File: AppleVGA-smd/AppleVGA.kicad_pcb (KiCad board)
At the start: 2 copper layers, 112.4 x 66.7 mm, 35 parts, among them J1 AppleIIBus, J2 VGA, Q1 DMG2305UX-7, SW1 Reset, U1 74LVC245, U2 74LVC245, U3 74LVC245, U4 74LVC245, U6 Pico

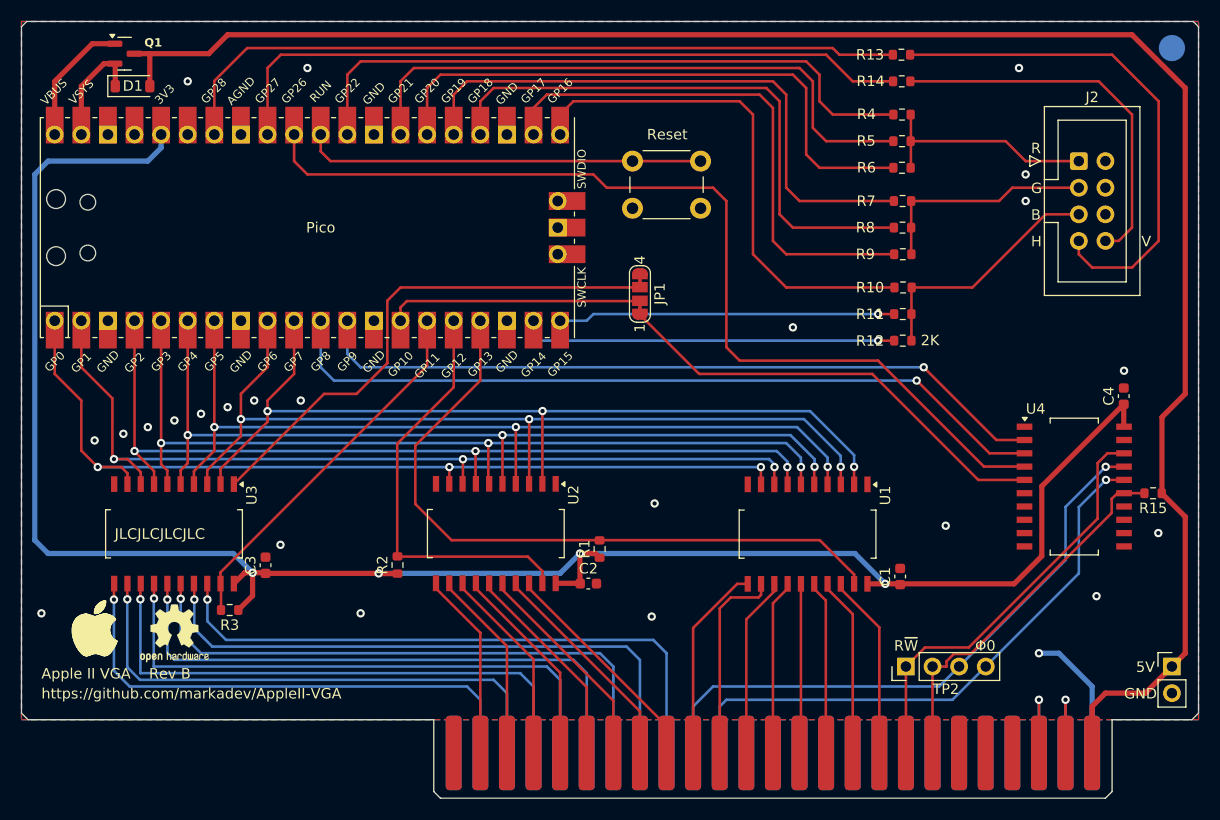
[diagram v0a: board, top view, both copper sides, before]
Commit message: Finalize SMD version
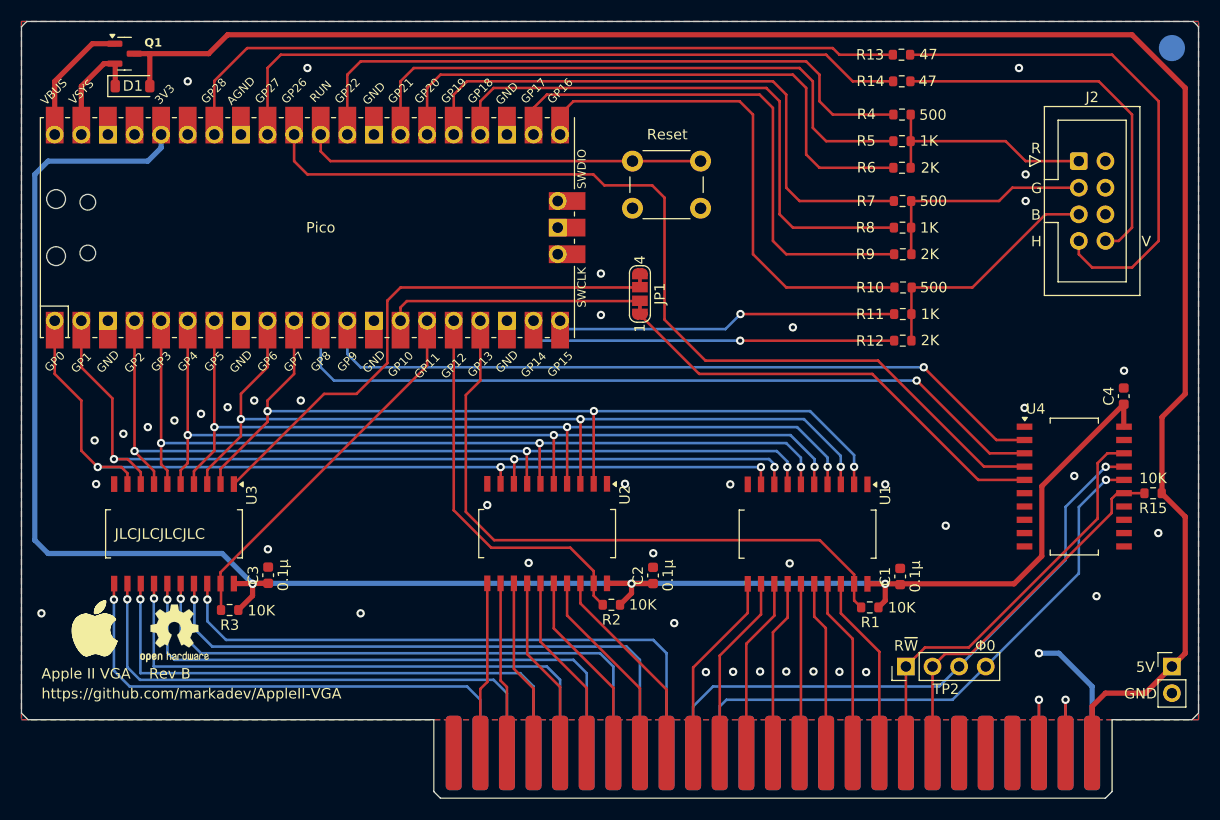
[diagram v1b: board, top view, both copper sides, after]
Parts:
- moved R1 26.4 mm to (161.7, 122.6), turned to 180 degrees
- moved R2 20.8 mm to (137.0, 122.4), turned to 180 degrees
- moved C2 6.22 mm to (140.9, 119.6), turned to 90 degrees
- moved U2 4.90 mm to (130.8, 115.6)
- moved C3 0.98 mm to (104.2, 119.5)
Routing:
- net Net-(U1-CE): track 65.7 -> 61.8 mm
- net Net-(U2-CE): track 40.4 -> 37.4 mm
- net /A2: track 19.6 -> 17.6 mm
- net /A3: track 20.2 -> 18.1 mm
- net /A7: track 22.3 -> 20.2 mm
- net /A1: track 19.1 -> 17.1 mm
- net /A9: track 20.0 -> 18.4 mm
- net /A6: track 21.7 -> 20.2 mm
- net /A5: track 21.2 -> 19.7 mm
- net /A0: track 18.6 -> 17.1 mm
- net /A4: track 20.7 -> 19.3 mm
- net PHI0_3.3: track 92.6 -> 91.2 mm
- net +3.3V: track 186.7 -> 185.7 mm, vias 4 -> 3
- net Net-(U6-GPIO15): track 32.2 -> 32.8 mm
- net /A8: track 19.5 -> 18.9 mm
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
